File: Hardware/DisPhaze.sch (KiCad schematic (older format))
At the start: 78 parts, among them J1 SWD_Header, J2 PItch_In, J3 PD1_Amt_In, J4 PD2_Amt_In, J5 VCA_In, J6 DAC1_Out, J7 DAC2_Out, J8 Eurorack_16_pin_power, SW1 DAC1_RingMod_Switch, SW2 DAC2_Mix_Switch, SW3 Octave_Switch, SW4 SW_Push, U1 STM32F405RGTx, U2 MCP6004, U3 TL072, U4 LM1117-3.3, Y1 Crystal

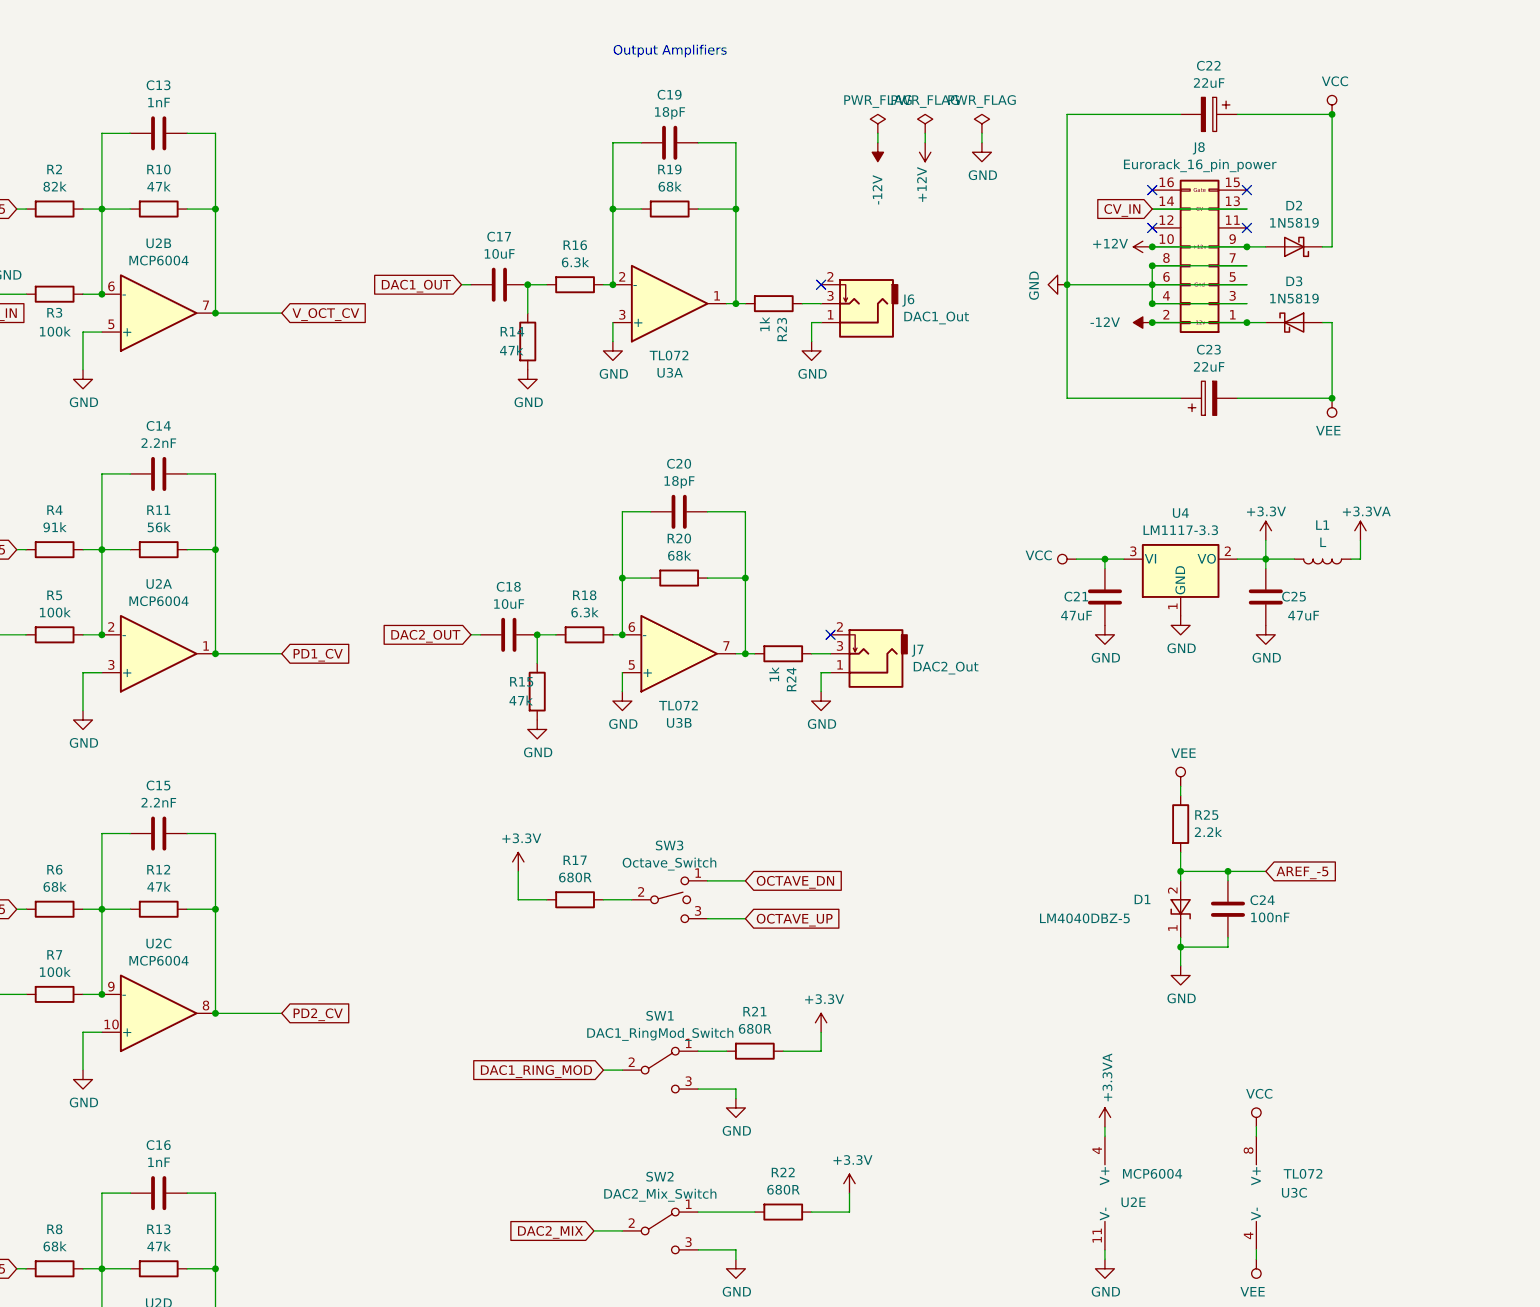
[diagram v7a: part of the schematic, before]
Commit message: Fixes to PCB silkscreen; Fixes to ADC function
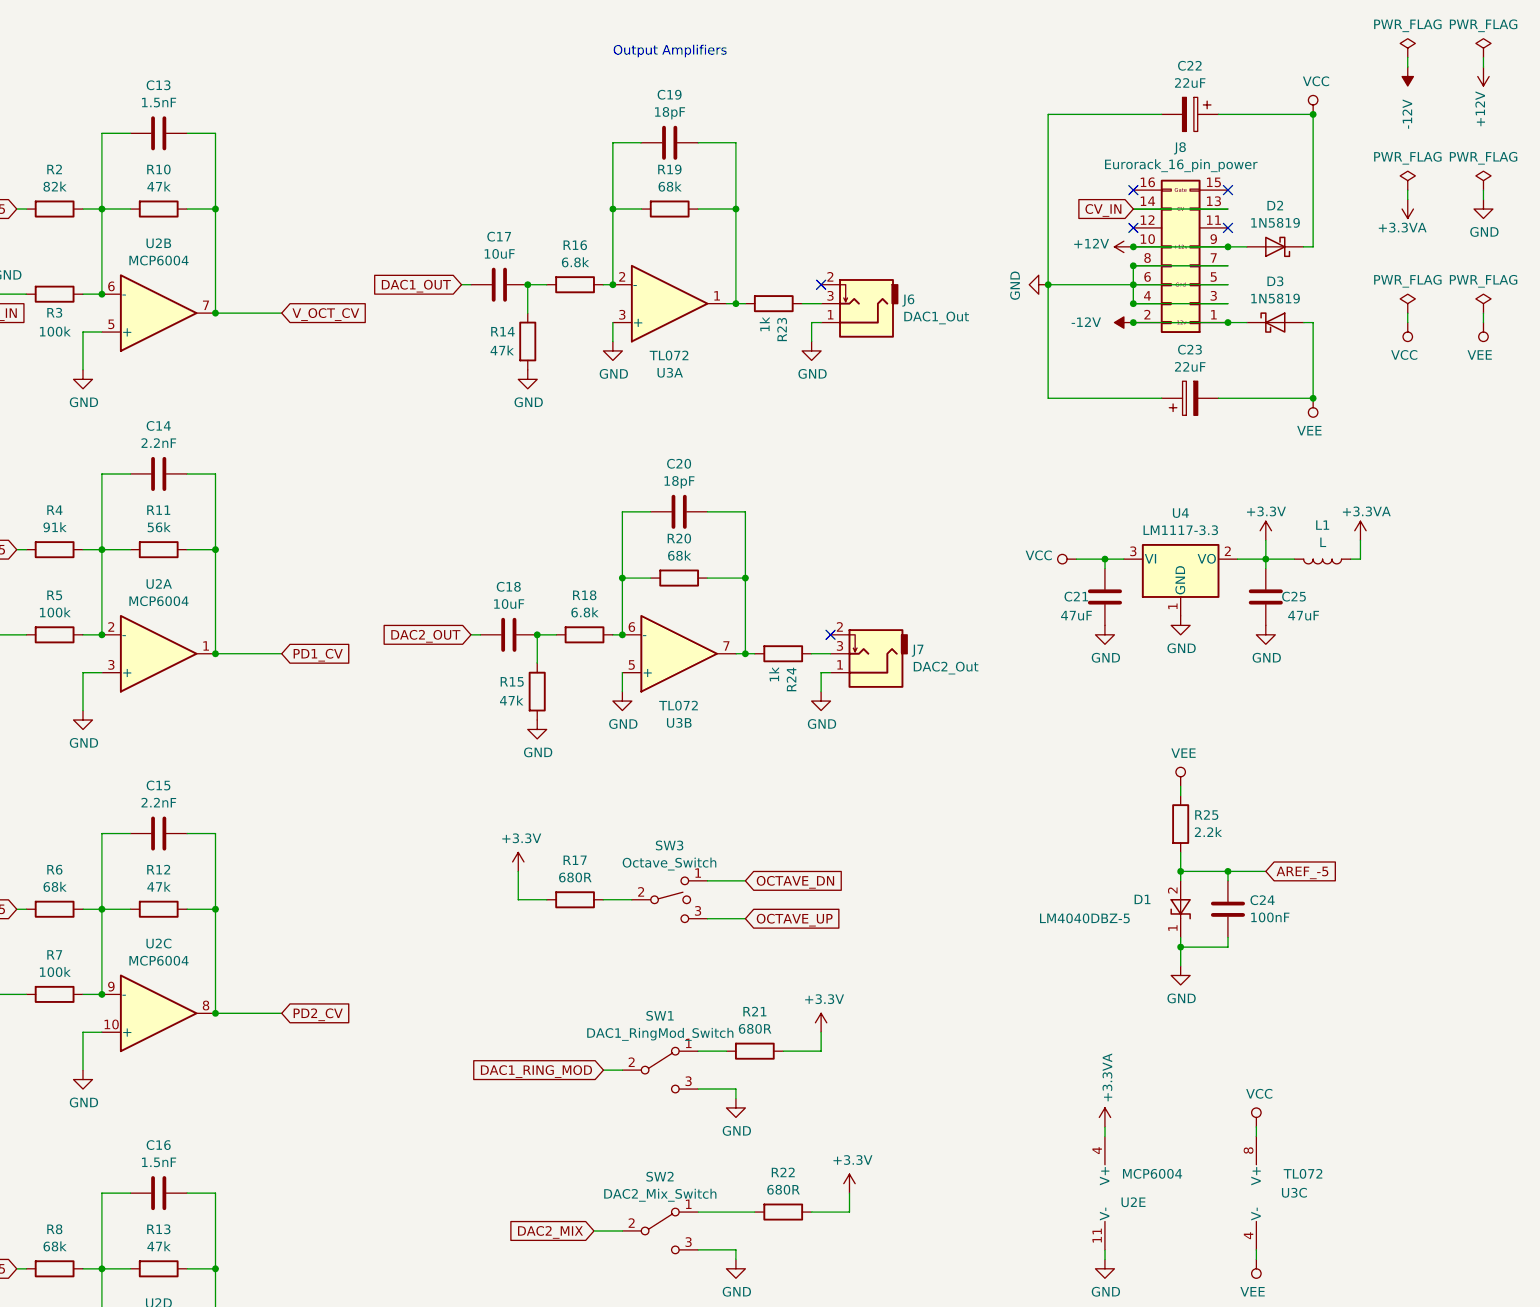
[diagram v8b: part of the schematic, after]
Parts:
- C13, C16: value 1nF -> 1.5nF
- CTune1, FTune1, PD1Amt1, PD1Type1, PD2Amt1, PD2Type1: footprint Potentiometers:Potentiometer_Alps_RK09K_Horizontal -> Custom_Footprints:Alpha_9mm_Potentiometer
- R16, R18: value 6.3k -> 6.8k
- SW4: footprint Buttons_Switches_SMD:SW_SPST_EVQQ2 -> Custom_Footprints:SW_SPST_EVQQ2
- Y1: footprint Crystals:Crystal_SMD_HC49-SD -> Custom_Footprints:Crystal_SMD
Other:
- moved on the sheet: C22, C23, D2, D3, J8
